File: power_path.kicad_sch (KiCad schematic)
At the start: 18 parts, among them J2 USB_C_Receptacle_USB2.0_16P, U2 TPS631000DRLR, U3 TLV77018PDBVR, U4 TPS2116DRL, U5 USBLC6-2SC6, U6 USBLC6-2SC6

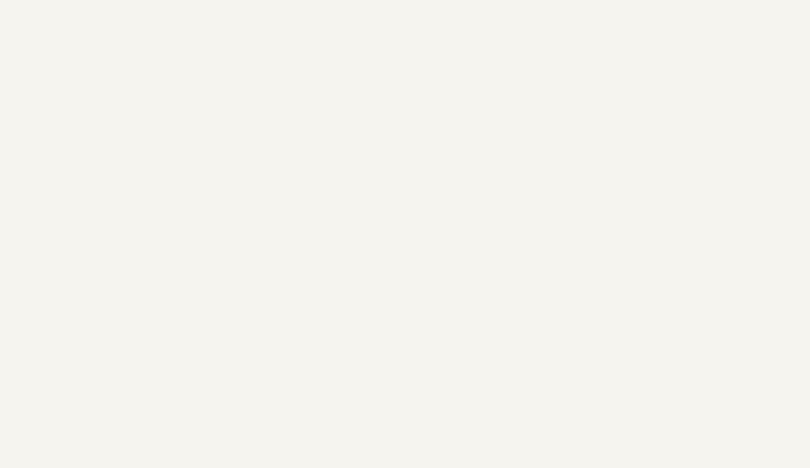
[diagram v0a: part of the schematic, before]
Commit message: add bq25302 charger
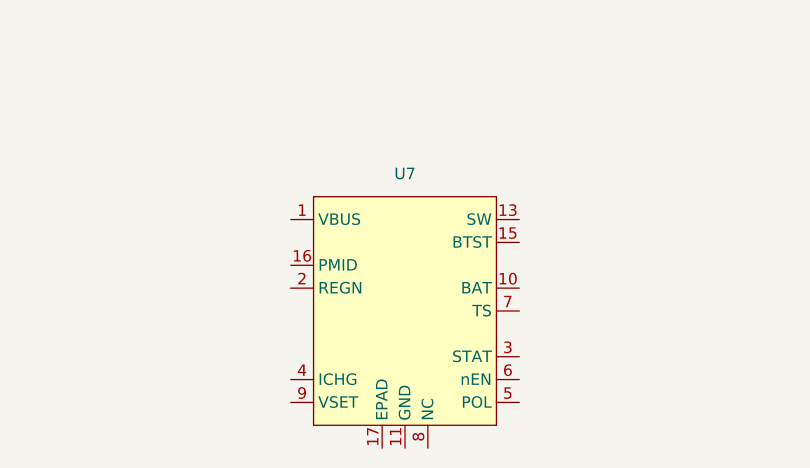
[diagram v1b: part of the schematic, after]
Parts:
- added U7: (no value), Package_DFN_QFN:WQFN-16-1EP_3x3mm_P0.5mm_EP1.68x1.68mm_ThermalVias, symbol symbols:BQ25302RTE
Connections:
- new net: U7.11 (GND), U7.12 (GND)
- new net: U7.13 (SW), U7.14 (SW)
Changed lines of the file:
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@@
+	)
+	(symbol
+		(lib_id "symbols:BQ25302RTE")
+		(at 129.54 137.16 0)
+		(unit 1)
+		(body_style 1)
+		(exclude_from_sim no)
+		(in_bom yes)
+		(on_board yes)
+		(in_pos_files yes)
+		(dnp no)
+		(fields_autoplaced yes)
+		(property "Reference" "U7"
+			(at 129.54 121.92 0)
+			(show_name no)
+			(do_not_autoplace no)
+			(effects
+				(font
+					(size 1.27 1.27)
+				)
+			)
+		)
+		(property "Value" ""
+			(at 129.54 137.16 0)
+			(show_name no)
+			(do_not_autoplace no)
+			(effects
+				(font
+					(size 1.27 1.27)
+				)
+			)
+		)
+		(property "Footprint" "Package_DFN_QFN:WQFN-16-1EP_3x3mm_P0.5mm_EP1.68x1.68mm_ThermalVias"
+			(at 129.54 137.16 0)
+			(hide yes)
+			(show_name no)
+			(do_not_autoplace no)
+			(effects
+				(font
+					(size 1.27 1.27)
+				)
+			)
+		)
+		(property "Datasheet" ""
+			(at 129.54 137.16 0)
+			(hide yes)
+			(show_name no)
+			(do_not_autoplace no)
+			(effects
+				(font
+					(size 1.27 1.27)
+				)
+			)
+		)
+		(property "Description" ""
+			(at 129.54 137.16 0)
+			(hide yes)
+			(show_name no)
+			(do_not_autoplace no)
+			(effects
+				(font
+					(size 1.27 1.27)
+				)
+			)
+		)
+		(property "LCSC" "C2761617"
+			(at 129.54 137.16 0)
+			(hide yes)
+			(show_name no)
+			(do_not_autoplace no)
+			(effects
+				(font
+					(size 1.27 1.27)
+				)
+			)
+		)
+		(pin "5"
+		)
+		(pin "3"
+		)
+		(pin "6"
+		)
+		(pin "2"
+		)
+		(pin "14"
+		)
+		(pin "13"
+		)
+		(pin "10"
+		)
+		(pin "17"
+		)
+		(pin "1"
+		)
+		(pin "15"
+		)
+		(pin "9"
+		)
+		(pin "8"
+		)
+		(pin "4"
+		)
+		(pin "12"
+		)
+		(pin "16"
+		)
+		(pin "7"
+		)
+		(pin "11"
+		)
+		(instances
+			(project "pedal"
+				(path "/e2443317-b83f-4e66-ac79-3186c6d613f3/487ab5a8-1c1d-4a3e-8f62-a21afc38e9a3"
+					(reference "U7")
+					(unit 1)
+				)
+			)
+		)
 	)
 	(symbol

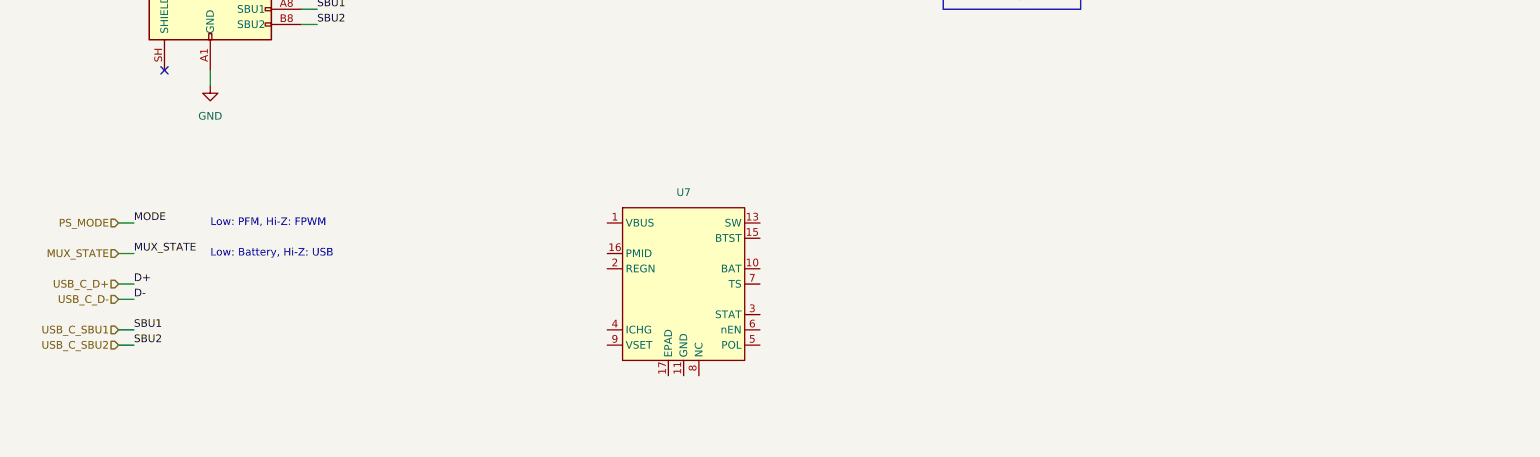
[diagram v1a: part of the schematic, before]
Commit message: charger supporting circuitry
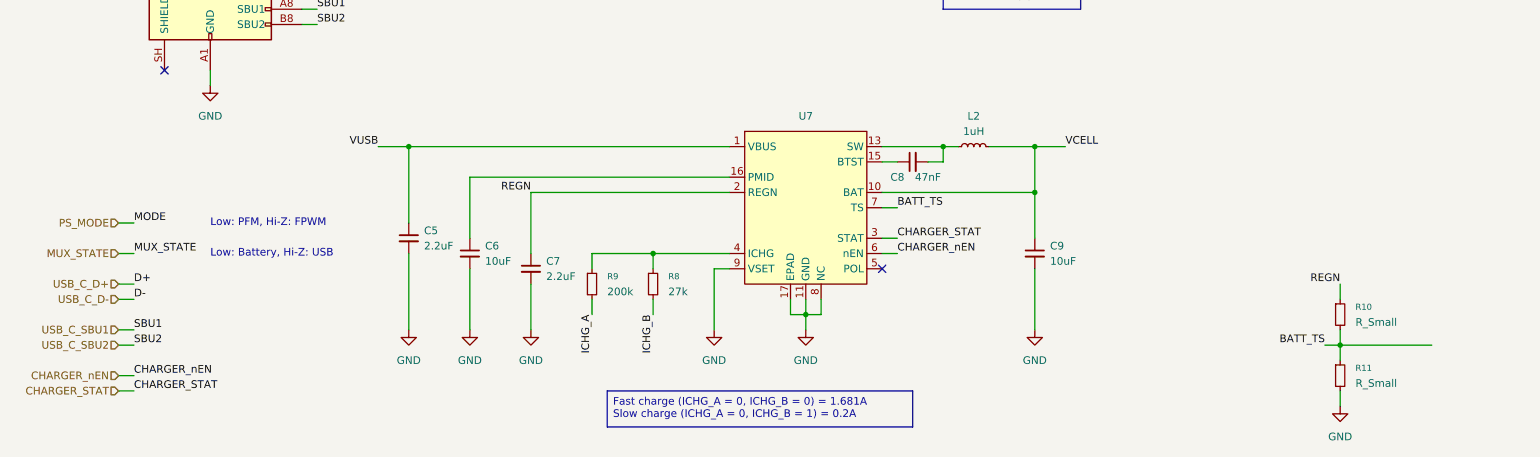
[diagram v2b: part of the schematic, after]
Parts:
- added C5, C7: 2.2uF, Capacitor_SMD:C_0603_1608Metric, symbol Device:C_Small
- added C6, C9: 10uF, Capacitor_SMD:C_0603_1608Metric, symbol Device:C_Small
- added C8: 47nF, Capacitor_SMD:C_0603_1608Metric, symbol Device:C_Small
- added L2: 1uH, Inductor_SMD:L_1008_2520Metric, symbol Device:L_Small
- added R10, R11: R_Small, symbol Device:R_Small
- added R8: 27k, Resistor_SMD:R_0402_1005Metric, symbol Device:R_Small
- added R9: 200k, Resistor_SMD:R_0402_1005Metric, symbol Device:R_Small
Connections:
- net GND: now also U7.11 (GND), U7.12 (GND), U7.17 (EPAD), U7.8 (NC), U7.9 (VSET), C5.2, C6.2, C7.2, C9.2, R11.2
- net VUSB: now also U7.1 (VBUS), C5.1
- net VCELL: now reaches U7.10 (BAT)
- net VCELL: now also C9.1, L2.2
- net at U7.13 (SW), U7.14 (SW): now also C8.2, L2.1
- net at U7.15 (BTST): now also C8.1
- net at U7.16 (PMID): now also C6.1
- net REGN: now reaches U7.2 (REGN)
- net REGN: now also C7.1, R10.1
- net CHARGER_STAT: now reaches U7.3 (STAT)
- net at U7.4 (ICHG): now also R8.1, R9.1
- net CHARGER_nEN: now reaches U7.6 (nEN)
- net BATT_TS: now reaches U7.7 (TS)
- net BATT_TS: now also R10.2, R11.1
- new net ICHG_A: R9.2
- new net ICHG_B: R8.2
- no-connect marks 1 -> 2
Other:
- moved on the sheet: U7

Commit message: fuel gauge wip
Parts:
- added BT1: Battery_Cell, symbol Device:Battery_Cell
- added C10: 1uF, Capacitor_SMD:C_0402_1005Metric, symbol Device:C_Small
- added C11: 2.2uF, Capacitor_SMD:C_0603_1608Metric, symbol Device:C_Small
- added SW1: SW_SPST, symbol Switch:SW_SPST
- added U8: BQ27427YZFR, BQ27427YZFR:IC_BQ27427YZFR, symbol symbols:BQ27427YZFR
- C4: voltage (none) -> 25
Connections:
- net VCELL is gone; now on net VBATT: C9.1, L2.2, U7.10 (BAT)
- net GND: now also BT1.2 (-), C10.2, C11.2, U8.B2 (VSS), U8.C1 (VSS)
- net VBATT: now also SW1.2 (B)
- net ICHG_A renamed CHARGER_ICHG_A
- net ICHG_B renamed CHARGER_ICHG_B
- new net: BT1.1 (+), C10.1, U8.C3 (BAT)
- new net: C11.1, U8.B3 (VDD)
- new net: SW1.1 (A), U8.C2 (SRX)
- new net FUEL_GAUGE_SCL: U8.A3 (SCL)
- new net FUEL_GAUGE_SDA: U8.A2 (SDA)
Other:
- note added: "switched battery?"
- moved on the sheet: R10, R11

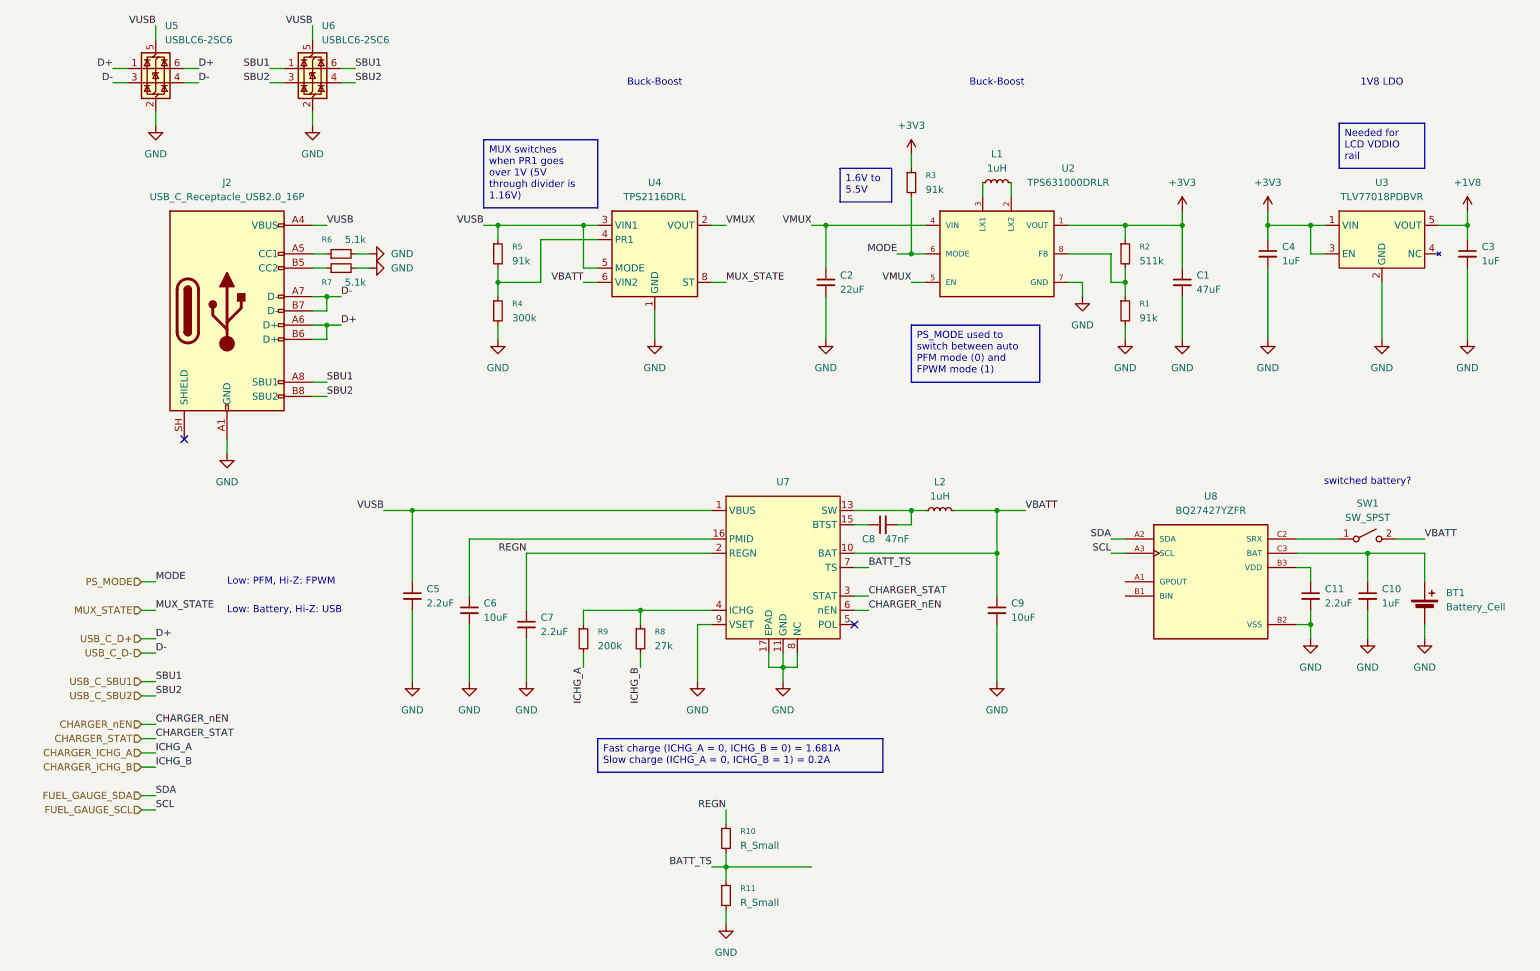
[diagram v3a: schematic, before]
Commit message: add switch for 3V3 enable
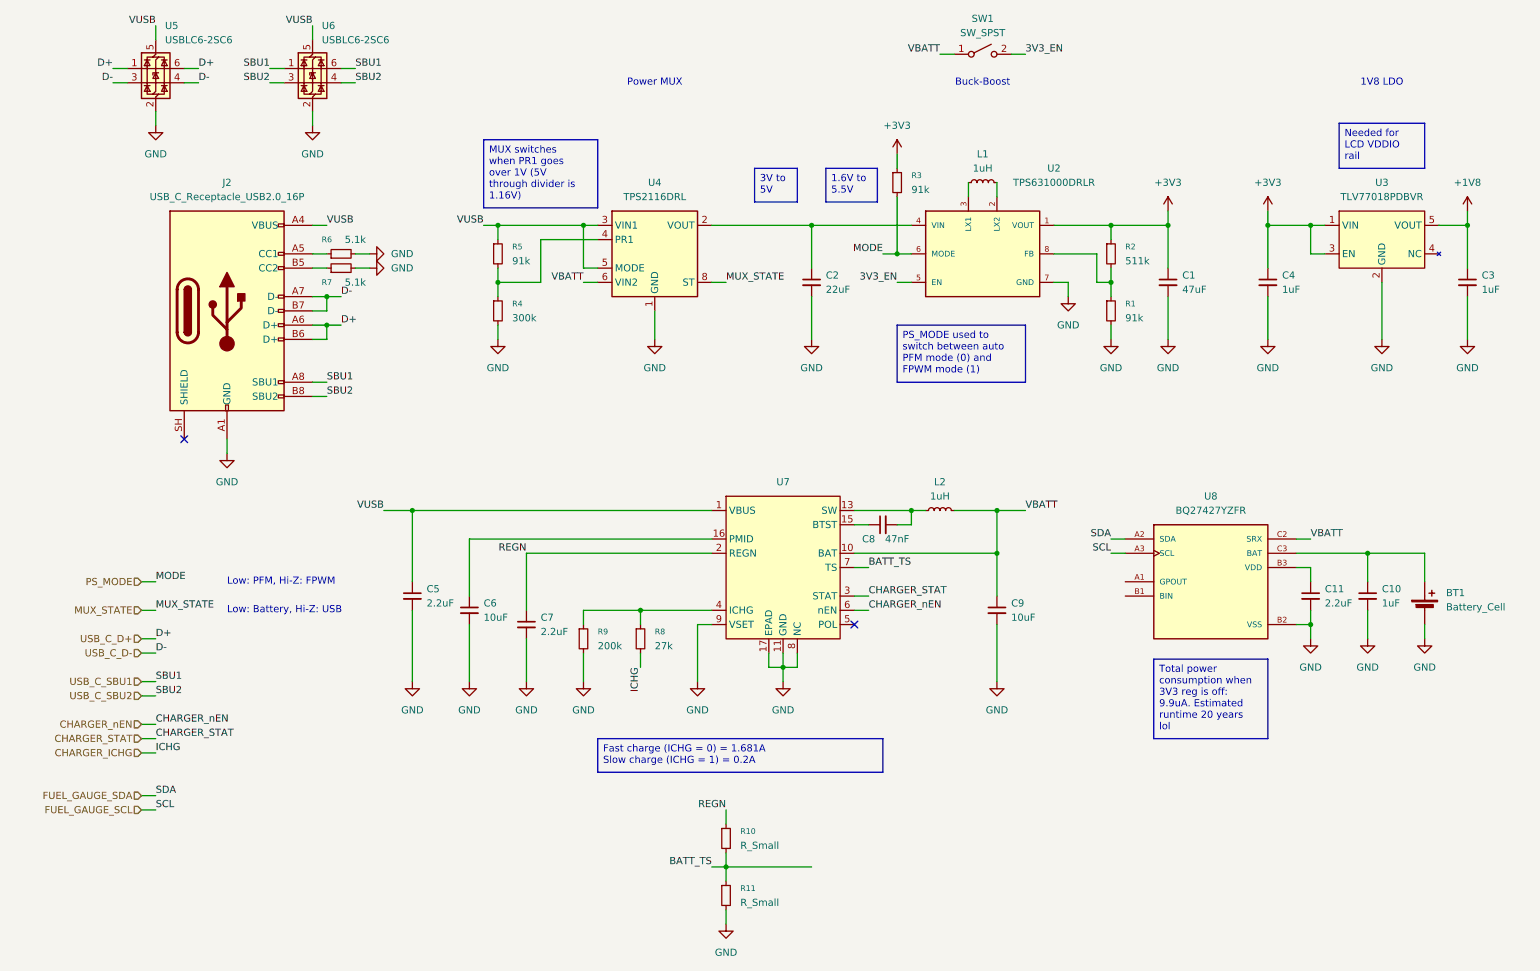
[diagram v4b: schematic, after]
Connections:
- net CHARGER_ICHG_A is gone; now on net GND: R9.2
- net VBATT: now also SW1.1 (A), U8.C2 (SRX); no longer SW1.2 (B)
- net CHARGER_ICHG_B renamed CHARGER_ICHG
- net VMUX: no longer names the net of C2.1, U2.4 (VIN), U4.2 (VOUT), U4.7 (VOUT)
- net VMUX: no longer U2.5 (EN)
- new net 3V3_EN: SW1.2 (B), U2.5 (EN)
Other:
- note added: "Power MUX"
- note removed: "switched battery?"
- moved on the sheet: C1, C2, C3, C4, L1, R1, R2, R3, U2

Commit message: vbatt is switched into power mux
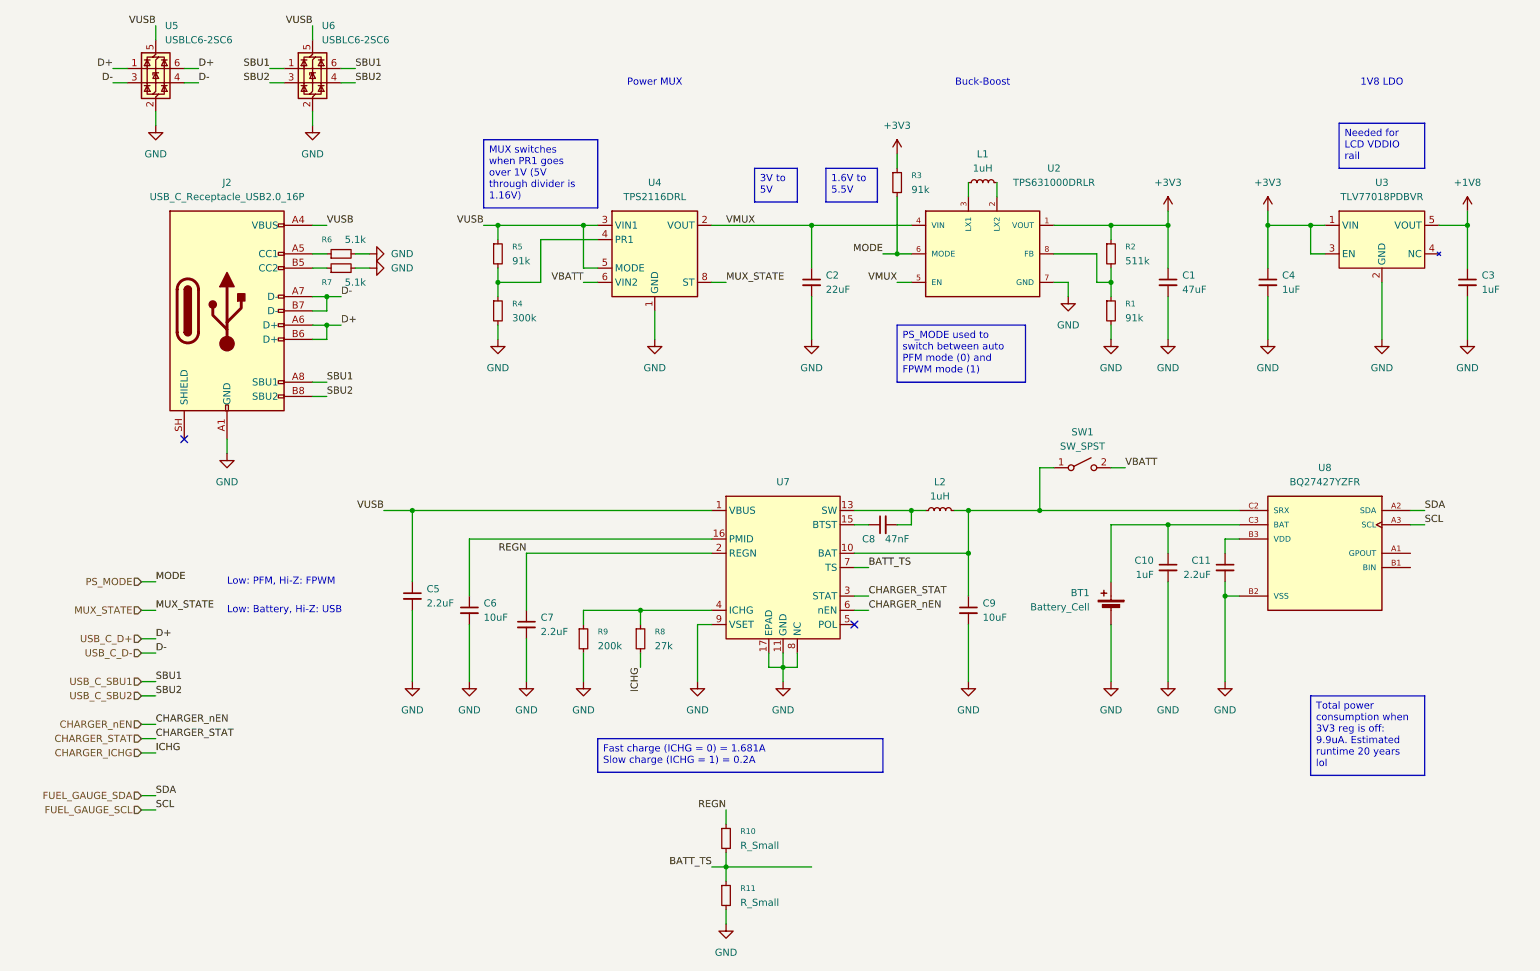
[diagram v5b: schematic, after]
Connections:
- net VBATT: now also SW1.2 (B); no longer C9.1, L2.2, SW1.1 (A), U7.10 (BAT), U8.C2 (SRX)
- net VMUX: now reaches C2.1, U2.4 (VIN), U4.2 (VOUT), U4.7 (VOUT)
- net VMUX: now also U2.5 (EN)
- removed net 3V3_EN: SW1.2 (B), U2.5 (EN)
- new net: C9.1, L2.2, SW1.1 (A), U7.10 (BAT), U8.C2 (SRX)
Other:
- moved on the sheet: BT1, C10, C11, C9, SW1, U8

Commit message: add switch model
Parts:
- SW1: LCSC (none) -> C22448008
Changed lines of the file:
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@@
+			)
+		)
+		(property "LCSC" "C22448008"
+			(at 203.2 106.68 0)
+			(hide yes)
+			(show_name no)
+			(do_not_autoplace no)
+			(effects
+				(font
+					(size 1.27 1.27)
+				)
 			)
 		)
